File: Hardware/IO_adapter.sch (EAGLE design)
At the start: 23 parts, among them Y1 32Khz

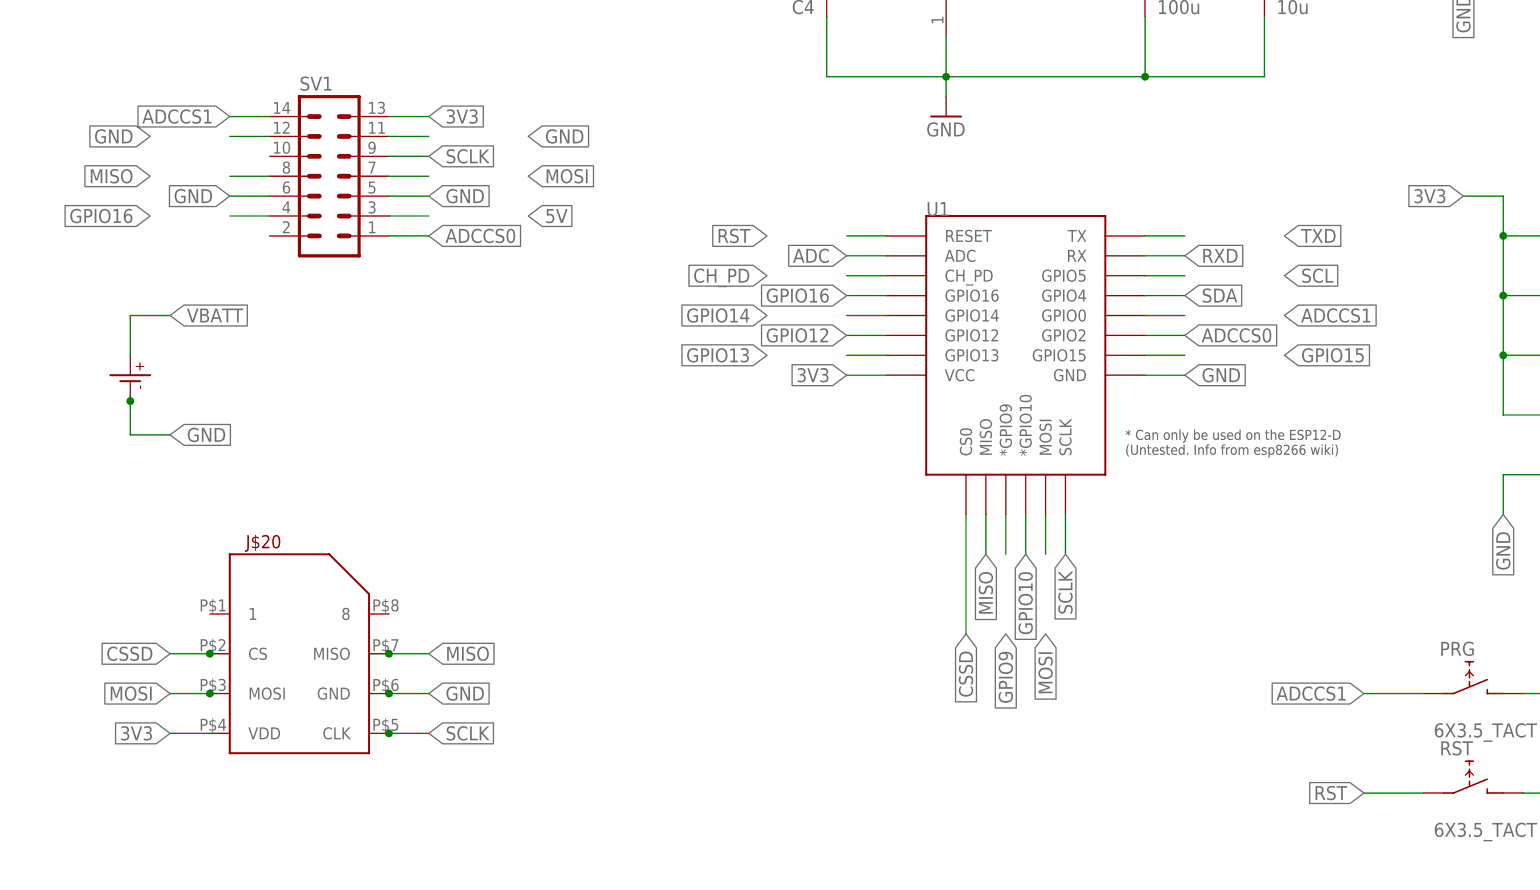
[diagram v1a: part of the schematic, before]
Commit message: corrected a major mistake
I had connected MOSI/MISO/SCLK to the primary hw SPI - now they are correctly conntected to the secondary bus.
MOSI->HSPI-D(GPIO13)
MISO->HSPI-Q(GPIO12)
SCLK->HSPI-CLK(GPIO14)
CSSD->HSPI-CD(GPIO15)

also added some minor changes to better fit the case
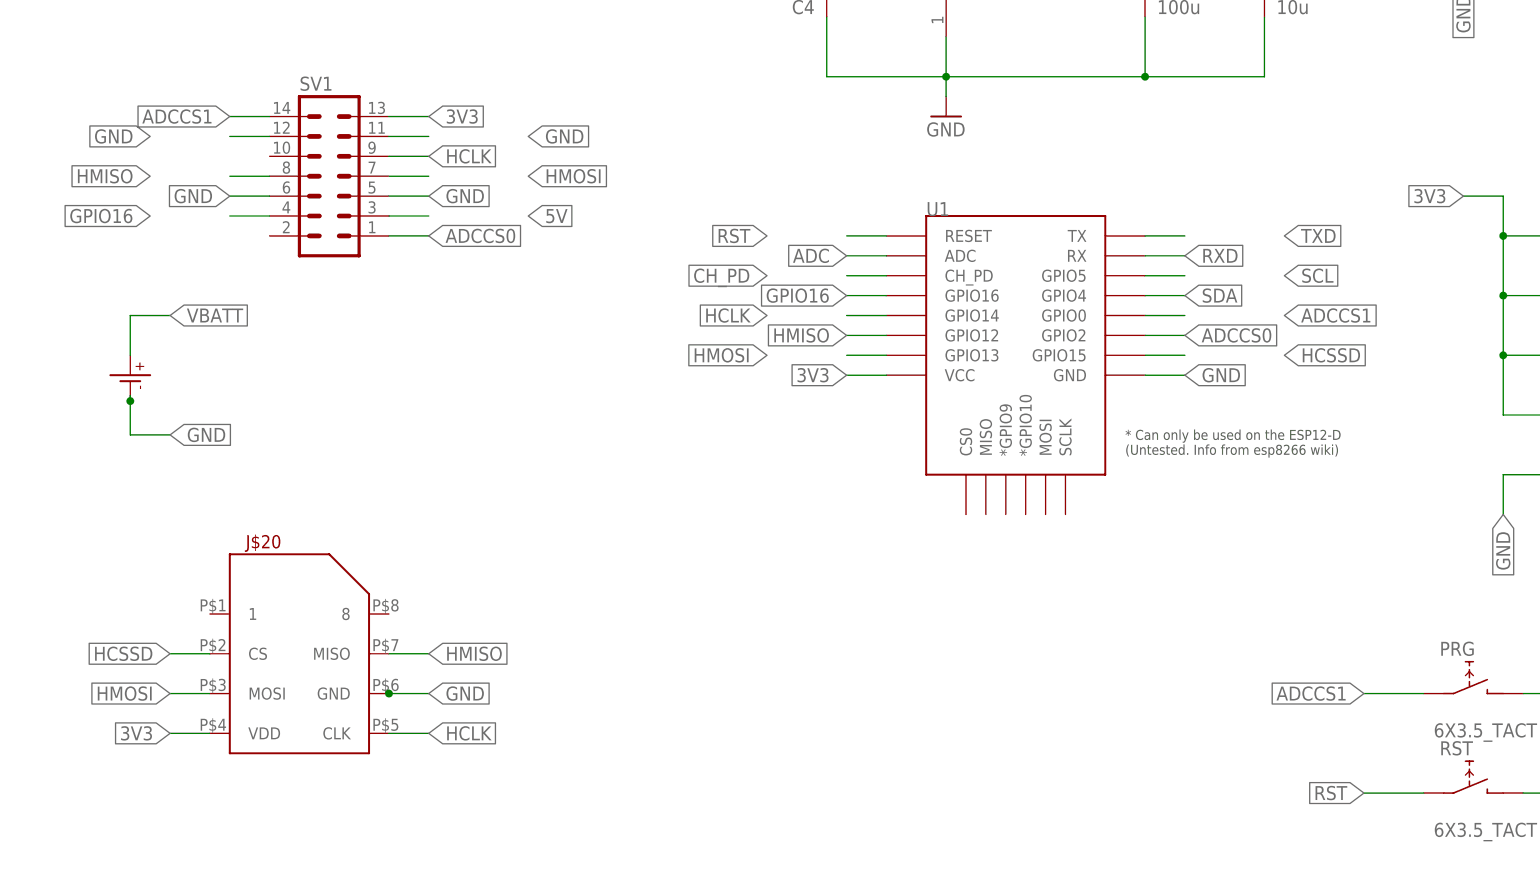
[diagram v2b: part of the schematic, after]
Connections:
- removed net CSSD: J$20.CS, U1.CS0
- removed net GPIO10: U1.*GPIO10
- removed net GPIO12: U1.GPIO12
- removed net GPIO13: U1.GPIO13
- removed net GPIO14: U1.GPIO14
- removed net GPIO9: U1.*GPIO9
- removed net MISO: J$20.MISO, SV1.8, U1.MISO
- removed net MOSI: J$20.MOSI, SV1.7, U1.MOSI
- removed net SCLK: J$20.CLK, SV1.9, U1.SCLK
- new net HCLK: J$20.CLK, SV1.9, U1.GPIO14
- new net HCSSD: J$20.CS, U1.GPIO15
- new net HMISO: J$20.MISO, SV1.8, U1.GPIO12
- new net HMOSI: J$20.MOSI, SV1.7, U1.GPIO13
- net GPIO15: no longer U1.GPIO15
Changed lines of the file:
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@@
-</segment>
-</net>
-<net name="MISO" class="0">
-<segment>
-<pinref part="J$20" gate="G$1" pin="MISO"/>
-<junction x="86.36" y="-48.26"/>
-<wire x1="86.36" y1="-48.26" x2="91.44" y2="-48.26" width="0.1524" layer="91"/>
-<label x="91.44" y="-48.26" size="1.778" layer="91" xref="yes"/>
-</segment>
-<segment>
-<pinref part="SV1" gate="G$1" pin="8"/>
-<wire x1="71.12" y1="12.7" x2="66.04" y2="12.7" width="0.1524" layer="91"/>
-<label x="55.88" y="12.7" size="1.778" layer="91" font="vector" rot="R180" xref="yes"/>
-</segment>
-<segment>
-<pinref part="U1" gate="G$1" pin="MISO"/>
-<wire x1="162.56" y1="-30.48" x2="162.56" y2="-35.56" width="0.1524" layer="91"/>
-<label x="162.56" y="-35.56" size="1.778" layer="91" rot="R270" xref="yes"/>
-</segment>
-</net>
-<net name="MOSI" class="0">
-<segment>
-<pinref part="J$20" gate="G$1" pin="MOSI"/>
-<junction x="63.5" y="-53.34"/>
-<wire x1="63.5" y1="-53.34" x2="58.42" y2="-53.34" width="0.1524" layer="91"/>
-<label x="58.42" y="-53.34" size="1.778" layer="91" rot="R180" xref="yes"/>
-</segment>
-<segment>
-<pinref part="SV1" gate="G$1" pin="7"/>
-<wire x1="86.36" y1="12.7" x2="91.44" y2="12.7" width="0.1524" layer="91"/>
-<label x="104.14" y="12.7" size="1.778" layer="91" font="vector" xref="yes"/>
-</segment>
-<segment>
-<pinref part="U1" gate="G$1" pin="MOSI"/>
-<wire x1="170.18" y1="-30.48" x2="170.18" y2="-35.56" width="0.1524" layer="91"/>
-<label x="170.18" y="-45.72" size="1.778" layer="91" rot="R270" xref="yes"/>
-</segment>
-</net>
-<net name="SCLK" class="0">
-<segment>
-<pinref part="J$20" gate="G$1" pin="CLK"/>
-<junction x="86.36" y="-58.42"/>
-<wire x1="86.36" y1="-58.42" x2="91.44" y2="-58.42" width="0.1524" layer="91"/>
-<label x="91.44" y="-58.42" size="1.778" layer="91" xref="yes"/>
-</segment>
-<segment>
-<pinref part="SV1" gate="G$1" pin="9"/>
-<wire x1="86.36" y1="15.24" x2="91.44" y2="15.24" width="0.1524" layer="91"/>
-<label x="91.44" y="15.24" size="1.778" layer="91" font="vector" xref="yes"/>
-</segment>
-<segment>
-<pinref part="U1" gate="G$1" pin="SCLK"/>
-<wire x1="172.72" y1="-30.48" x2="172.72" y2="-35.56" width="0.1524" layer="91"/>
-<label x="172.72" y="-35.56" size="1.778" layer="91" rot="R270" xref="yes"/>
 </segment>
 </net>
@@
 </segment>
 </net>
-<net name="CSSD" class="0">
-<segment>
-<pinref part="J$20" gate="G$1" pin="CS"/>
-<junction x="63.5" y="-48.26"/>
-<wire x1="63.5" y1="-48.26" x2="58.42" y2="-48.26" width="0.1524" layer="91"/>
-<label x="58.42" y="-48.26" size="1.778" layer="91" rot="R180" xref="yes"/>
-</segment>
-<segment>
-<pinref part="U1" gate="G$1" pin="CS0"/>
-<wire x1="160.02" y1="-30.48" x2="160.02" y2="-45.72" width="0.1524" layer="91"/>
-<label x="160.02" y="-45.72" size="1.778" layer="91" rot="R270" xref="yes"/>
-</segment>
-</net>
 <net name="N$8" class="0">
 <segment>
@@
 </segment>
 </net>
-<net name="GPIO14" class="0">
+<net name="HCLK" class="0">
 <segment>
 <pinref part="U1" gate="G$1" pin="GPIO14"/>
@@
 <label x="134.62" y="-5.08" size="1.778" layer="91" rot="R180" xref="yes"/>
 </segment>
-</net>
-<net name="GPIO12" class="0">
+<segment>
+<pinref part="J$20" gate="G$1" pin="CLK"/>
+<wire x1="86.36" y1="-58.42" x2="91.44" y2="-58.42" width="0.1524" layer="91"/>
+<label x="91.44" y="-58.42" size="1.778" layer="95" xref="yes"/>
+</segment>
+<segment>
+<pinref part="SV1" gate="G$1" pin="9"/>
+<wire x1="86.36" y1="15.24" x2="91.44" y2="15.24" width="0.1524" layer="91"/>
+<label x="91.44" y="15.24" size="1.778" layer="91" font="vector" xref="yes"/>
+</segment>
+</net>
+<net name="HMISO" class="0">
 <segment>
 <pinref part="U1" gate="G$1" pin="GPIO12"/>
@@
 <label x="144.78" y="-7.62" size="1.778" layer="91" rot="R180" xref="yes"/>
 </segment>
-</net>
-<net name="GPIO13" class="0">
+<segment>
+<pinref part="J$20" gate="G$1" pin="MISO"/>
+<wire x1="86.36" y1="-48.26" x2="91.44" y2="-48.26" width="0.1524" layer="91"/>
+<label x="91.44" y="-48.26" size="1.778" layer="95" xref="yes"/>
+</segment>
+<segment>
+<pinref part="SV1" gate="G$1" pin="8"/>
+<wire x1="71.12" y1="12.7" x2="66.04" y2="12.7" width="0.1524" layer="91"/>
+<label x="55.88" y="12.7" size="1.778" layer="91" font="vector" rot="R180" xref="yes"/>
+</segment>
+</net>
+<net name="HMOSI" class="0">
 <segment>
 <pinref part="U1" gate="G$1" pin="GPIO13"/>
@@
 <label x="134.62" y="-10.16" size="1.778" layer="91" rot="R180" xref="yes"/>
 </segment>
+<segment>
+<pinref part="J$20" gate="G$1" pin="MOSI"/>
+<wire x1="63.5" y1="-53.34" x2="58.42" y2="-53.34" width="0.1524" layer="91"/>
+<label x="58.42" y="-53.34" size="1.778" layer="95" rot="R180" xref="yes"/>
+</segment>
+<segment>
+<pinref part="SV1" gate="G$1" pin="7"/>
+<wire x1="86.36" y1="12.7" x2="91.44" y2="12.7" width="0.1524" layer="91"/>
+<label x="104.14" y="12.7" size="1.778" layer="91" font="vector" xref="yes"/>
+</segment>
 </net>
 <net name="TXD" class="0">
@@
 <net name="GPIO15" class="0">
 <segment>
-<pinref part="U1" gate="G$1" pin="GPIO15"/>
-<wire x1="182.88" y1="-10.16" x2="187.96" y2="-10.16" width="0.1524" layer="91"/>
-<label x="200.66" y="-10.16" size="1.778" layer="91" xref="yes"/>
-</segment>
-<segment>
 <pinref part="R8" gate="G$1" pin="2"/>
 <wire x1="251.46" y1="-25.4" x2="261.62" y2="-25.4" width="0.1524" layer="91"/>
 <label x="261.62" y="-25.4" size="1.778" layer="91" font="vector" xref="yes"/>
-</segment>
-</net>
-<net name="GPIO9" class="0">
-<segment>
-<pinref part="U1" gate="G$1" pin="*GPIO9"/>
-<wire x1="165.1" y1="-30.48" x2="165.1" y2="-35.56" width="0.1524" layer="91"/>
-<label x="165.1" y="-45.72" size="1.778" layer="91" rot="R270" xref="yes"/>
-</segment>
-</net>
-<net name="GPIO10" class="0">
-<segment>
-<pinref part="U1" gate="G$1" pin="*GPIO10"/>
-<wire x1="167.64" y1="-30.48" x2="167.64" y2="-35.56" width="0.1524" layer="91"/>
-<label x="167.64" y="-35.56" size="1.778" layer="91" rot="R270" xref="yes"/>
 </segment>
 </net>
@@
 </segment>
 </net>
+<net name="HCSSD" class="0">
+<segment>
+<pinref part="U1" gate="G$1" pin="GPIO15"/>
+<wire x1="182.88" y1="-10.16" x2="187.96" y2="-10.16" width="0.1524" layer="91"/>
+<label x="200.66" y="-10.16" size="1.778" layer="91" xref="yes"/>
+</segment>
+<segment>
+<pinref part="J$20" gate="G$1" pin="CS"/>
+<wire x1="63.5" y1="-48.26" x2="58.42" y2="-48.26" width="0.1524" layer="91"/>
+<label x="58.42" y="-48.26" size="1.778" layer="95" rot="R180" xref="yes"/>
+</segment>
+</net>

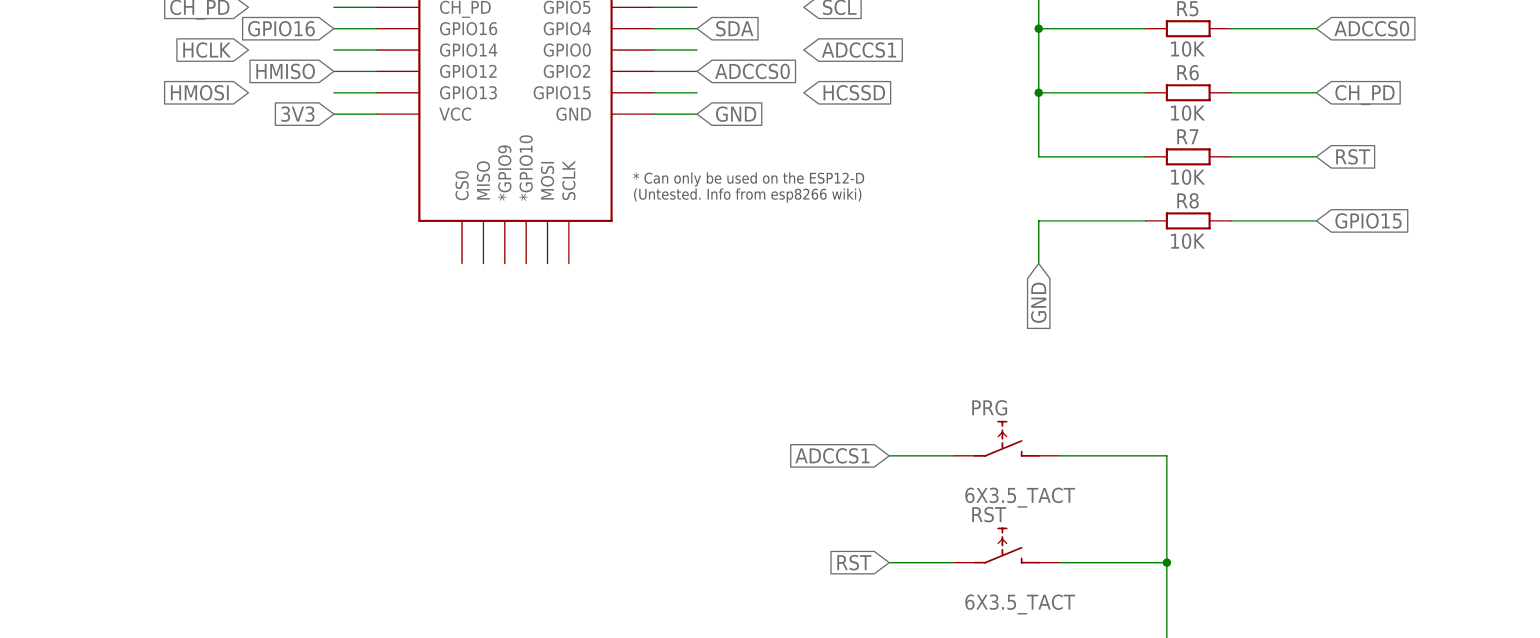
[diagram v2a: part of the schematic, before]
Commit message: SPI termination resistor positions
added SPI termination resistor positions
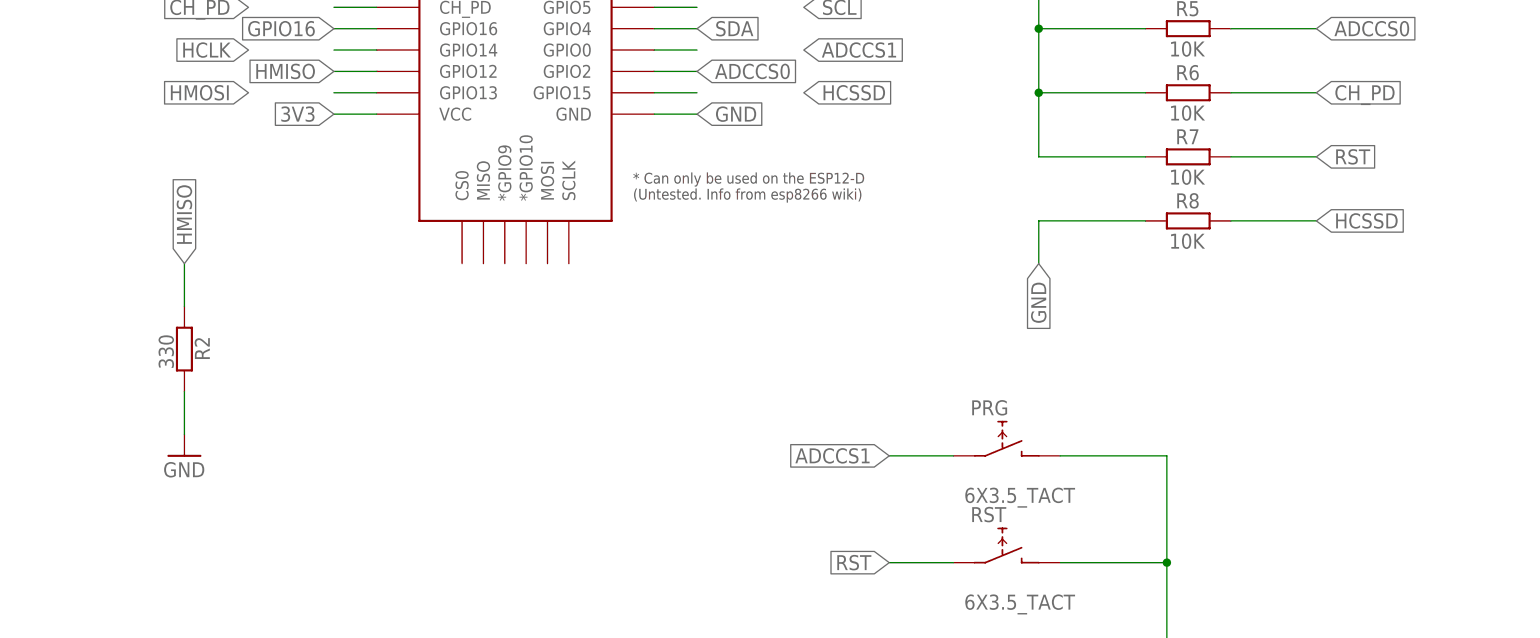
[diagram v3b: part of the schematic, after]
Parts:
- added R2: 330, resistor:R-EU_R0805
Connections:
- removed net GPIO15: R8.2
- net GND: now also R2.2
- net HCSSD: now also R8.2
- net HMISO: now also R2.1
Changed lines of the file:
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@@
 <part name="JP1" library="pinhead" deviceset="PINHD-1X4" device=""/>
 <part name="FRAME1" library="frames" deviceset="DINA3_L" device=""/>
+<part name="R2" library="resistor" deviceset="R-EU_" device="R0805" value="330"/>
+<part name="GND2" library="supply1" deviceset="GND" device=""/>
 </parts>
 <sheets>
@@
 <instance part="FRAME1" gate="G$1" x="-10.16" y="-142.24"/>
 <instance part="FRAME1" gate="G$2" x="276.86" y="-142.24"/>
+<instance part="R2" gate="G$1" x="127" y="-40.64" smashed="yes" rot="R270">
+<attribute name="NAME" x="128.2446" y="-39.116" size="1.778" layer="95" rot="R270"/>
+<attribute name="VALUE" x="123.952" y="-38.862" size="1.778" layer="96" rot="R270"/>
+</instance>
+<instance part="GND2" gate="1" x="127" y="-53.34"/>
 </instances>
 <busses>
@@
 <pinref part="JP1" gate="A" pin="4"/>
 <wire x1="246.38" y1="27.94" x2="254" y2="27.94" width="0.1524" layer="91"/>
+</segment>
+<segment>
+<pinref part="GND2" gate="1" pin="GND"/>
+<pinref part="R2" gate="G$1" pin="2"/>
+<wire x1="127" y1="-50.8" x2="127" y2="-45.72" width="0.1524" layer="91"/>
 </segment>
 </net>
@@
 <label x="55.88" y="12.7" size="1.778" layer="91" font="vector" rot="R180" xref="yes"/>
 </segment>
+<segment>
+<pinref part="R2" gate="G$1" pin="1"/>
+<wire x1="127" y1="-35.56" x2="127" y2="-30.48" width="0.1524" layer="91"/>
+<label x="127" y="-30.48" size="1.778" layer="95" rot="R90" xref="yes"/>
+</segment>
 </net>
 <net name="HMOSI" class="0">
@@
 <pinref part="JP1" gate="A" pin="2"/>
 <wire x1="246.38" y1="22.86" x2="254" y2="22.86" width="0.1524" layer="91"/>
-</segment>
-</net>
-<net name="GPIO15" class="0">
-<segment>
-<pinref part="R8" gate="G$1" pin="2"/>
-<wire x1="251.46" y1="-25.4" x2="261.62" y2="-25.4" width="0.1524" layer="91"/>
-<label x="261.62" y="-25.4" size="1.778" layer="91" font="vector" xref="yes"/>
 </segment>
 </net>
@@
 <label x="58.42" y="-48.26" size="1.778" layer="95" rot="R180" xref="yes"/>
 </segment>
-</net>
+<segment>
+<pinref part="R8" gate="G$1" pin="2"/>
+<wire x1="251.46" y1="-25.4" x2="261.62" y2="-25.4" width="0.1524" layer="91"/>
+<label x="261.62" y="-25.4" size="1.778" layer="91" font="vector" xref="yes"/>
+</segment>
+</net>

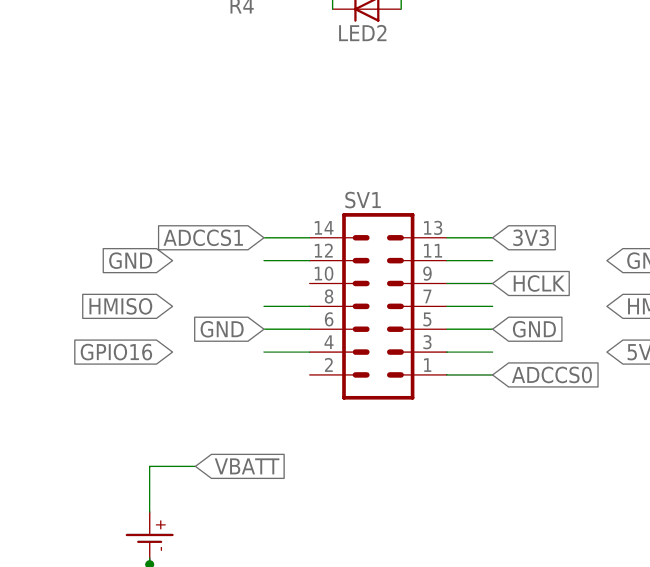
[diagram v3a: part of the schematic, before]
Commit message: mechanical fitting
moved the clamp positions such that they should fit unmodified.
Added silkscreen signal names for the power board ribbon connector, improved 3V3 connection on IO Board
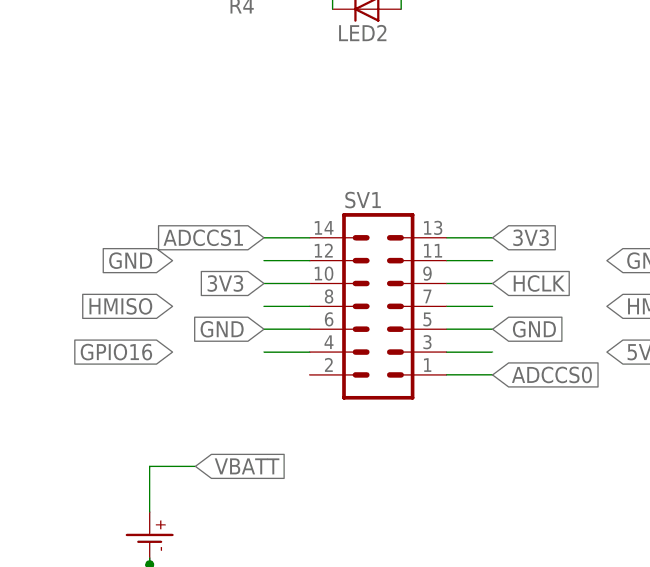
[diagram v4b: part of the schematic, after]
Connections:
- net 3V3: now also SV1.10
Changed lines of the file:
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@@
 <wire x1="246.38" y1="20.32" x2="254" y2="20.32" width="0.1524" layer="91"/>
+</segment>
+<segment>
+<pinref part="SV1" gate="G$1" pin="10"/>
+<wire x1="71.12" y1="15.24" x2="66.04" y2="15.24" width="0.1524" layer="91"/>
+<label x="66.04" y="15.24" size="1.778" layer="95" rot="R180" xref="yes"/>
 </segment>
 </net>
